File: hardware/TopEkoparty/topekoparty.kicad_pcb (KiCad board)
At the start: 2 copper layers, 88.5 x 27.8 mm, 5 parts

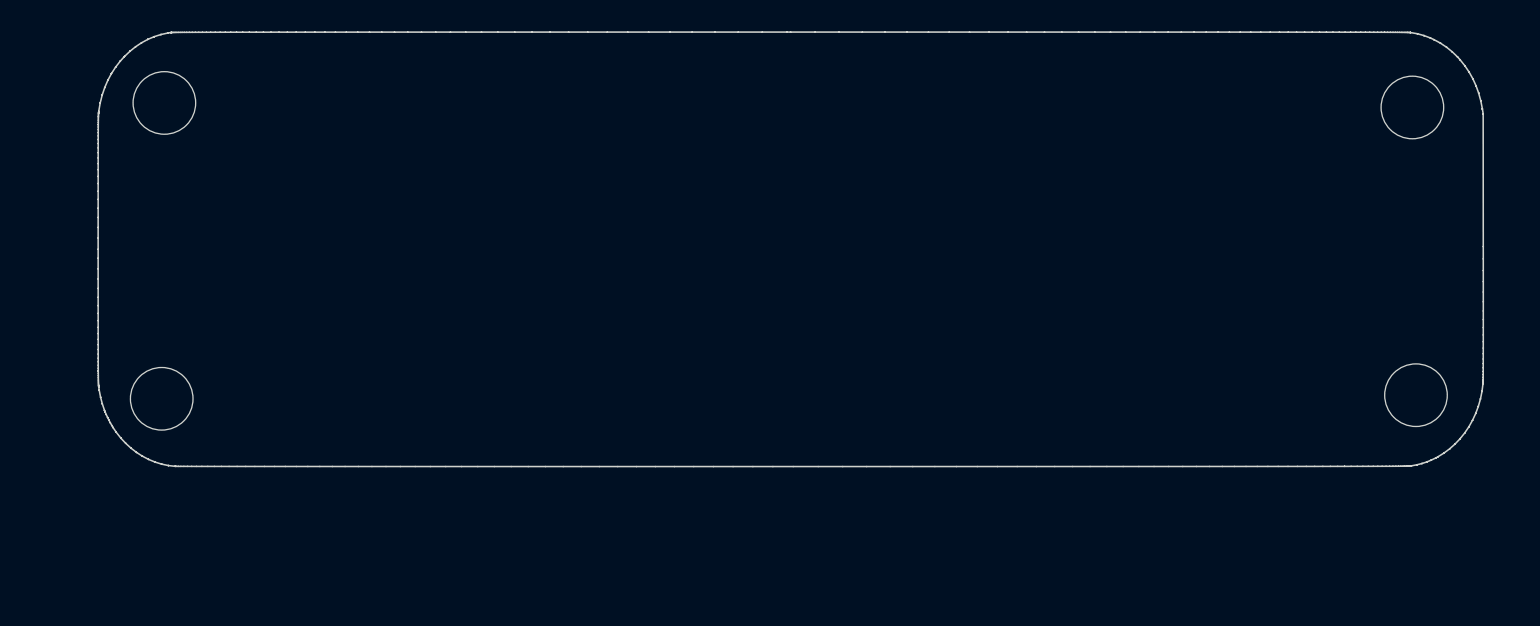
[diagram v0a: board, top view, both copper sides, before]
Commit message: Change the design of the top part of the badge
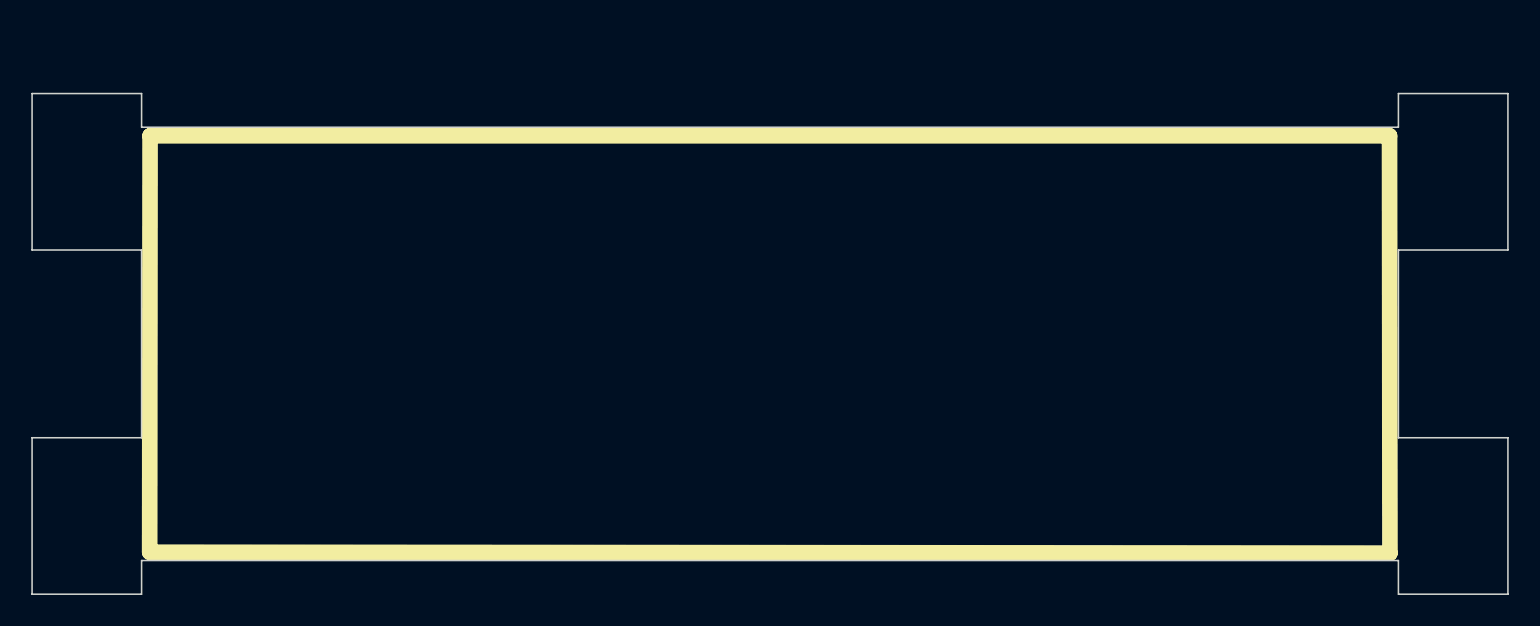
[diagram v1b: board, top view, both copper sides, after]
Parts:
- removed ? (x2): , 
- removed REF** (x2): Tornillo, TopEkoparty:Tornillo
- removed the Ref** at (154.6, 92.2)
- added Ref**: Val**, TopEkoparty:Top, F.Cu at (150.8, 92.2)
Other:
- board size 88.5 x 27.8 mm -> 94.3 x 32 mm

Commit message: Starting to route
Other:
- board text added: "thickness 0.7mm"
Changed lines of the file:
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@@
       (stroke (width 0.1) (type default)) (layer "Edge.Cuts"))
   )
+  (gr_text "thickness 0.7mm" (at 125.95 71.97) (layer "Eco1.User")
+    (effects (font (size 4 4) (thickness 0.3) bold) (justify left bottom))
+  )
 )

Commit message: add copper to the top badge
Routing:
- added copper zone on B.Cu, net (none)
- added copper zone on F.Cu, net (none)
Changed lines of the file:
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@@
     (effects (font (size 4 4) (thickness 0.3) bold) (justify left bottom))
   )
+  (zone (net 0) (net_name "") (layers "F&B.Cu") (hatch edge 0.5)
+    (connect_pads (clearance 0))
+    (min_thickness 0.25) (filled_areas_thickness no)
+    (keepout (tracks not_allowed) (vias not_allowed) (pads not_allowed) (copperpour not_allowed) (footprints allowed))
+    (fill (thermal_gap 0.5) (thermal_bridge_width 0.5))
+    (polygon
+      (pts
+        (xy 113.92 84.39)
+        (xy 188.86 84.16)
+        (xy 188.86 99.68)
+        (xy 113.81 99.79)
+      )
+    )
+  )
+  (zone (net 0) (net_name "") (layers "F&B.Cu") (hatch edge 0.5)
+    (connect_pads (clearance 0.5))
+    (min_thickness 0.25) (filled_areas_thickness no)
+    (fill yes (thermal_gap 0.5) (thermal_bridge_width 0.5) (island_removal_mode 1) (island_area_min 10))
+    (polygon
+      (pts
+        (xy 111.38 79.06)
+        (xy 190.01 78.83)
+        (xy 190.25 105.58)
+        (xy 110.91 105.81)
+        (xy 111.03 104.54)
+      )
+    )
+  )
 )

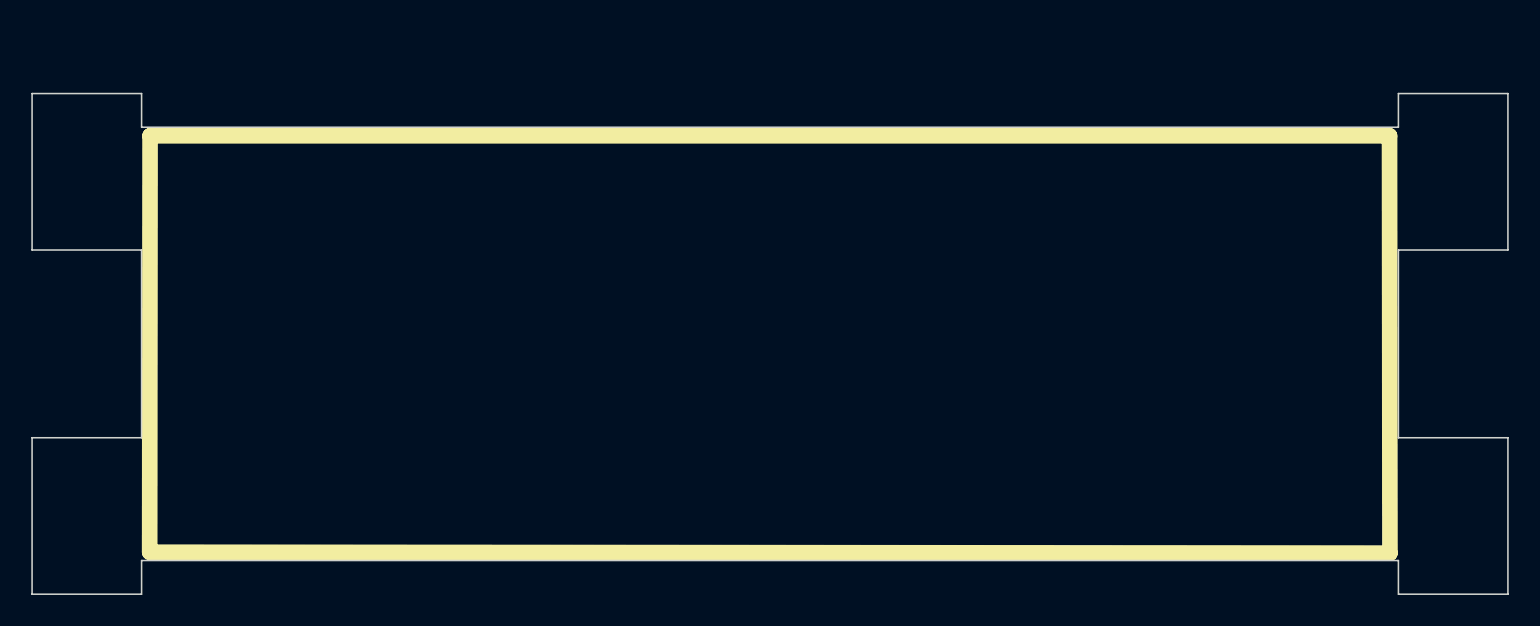
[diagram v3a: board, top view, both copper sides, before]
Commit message: hanging hole moved up and started modification of top part of the badge
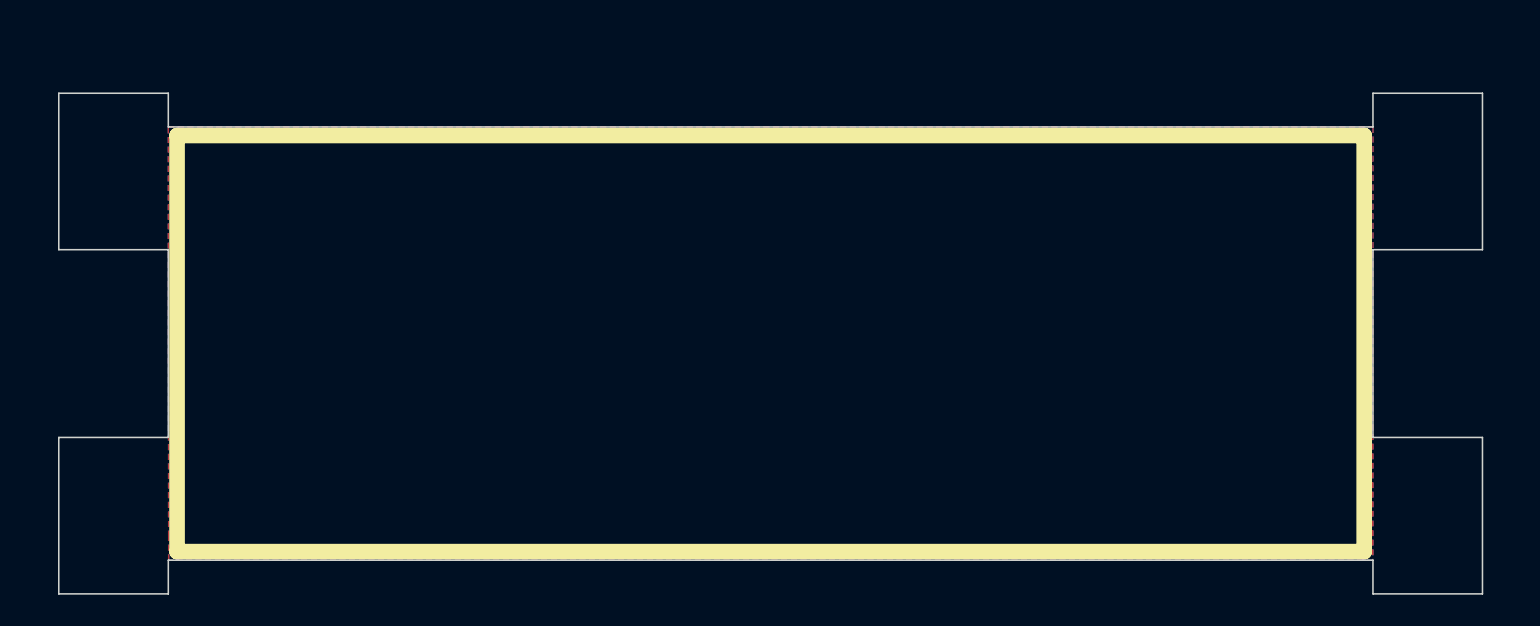
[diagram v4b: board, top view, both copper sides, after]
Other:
- board size 94.3 x 32 mm -> 91 x 32 mm
- board text added: "thickness 0.6mm"
- board text removed: "thickness 0.7mm"
